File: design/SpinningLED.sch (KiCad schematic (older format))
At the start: 26 parts, among them IC1 4069, IC2 4017, P1 +, P2 -, SW1 SW_PUSH

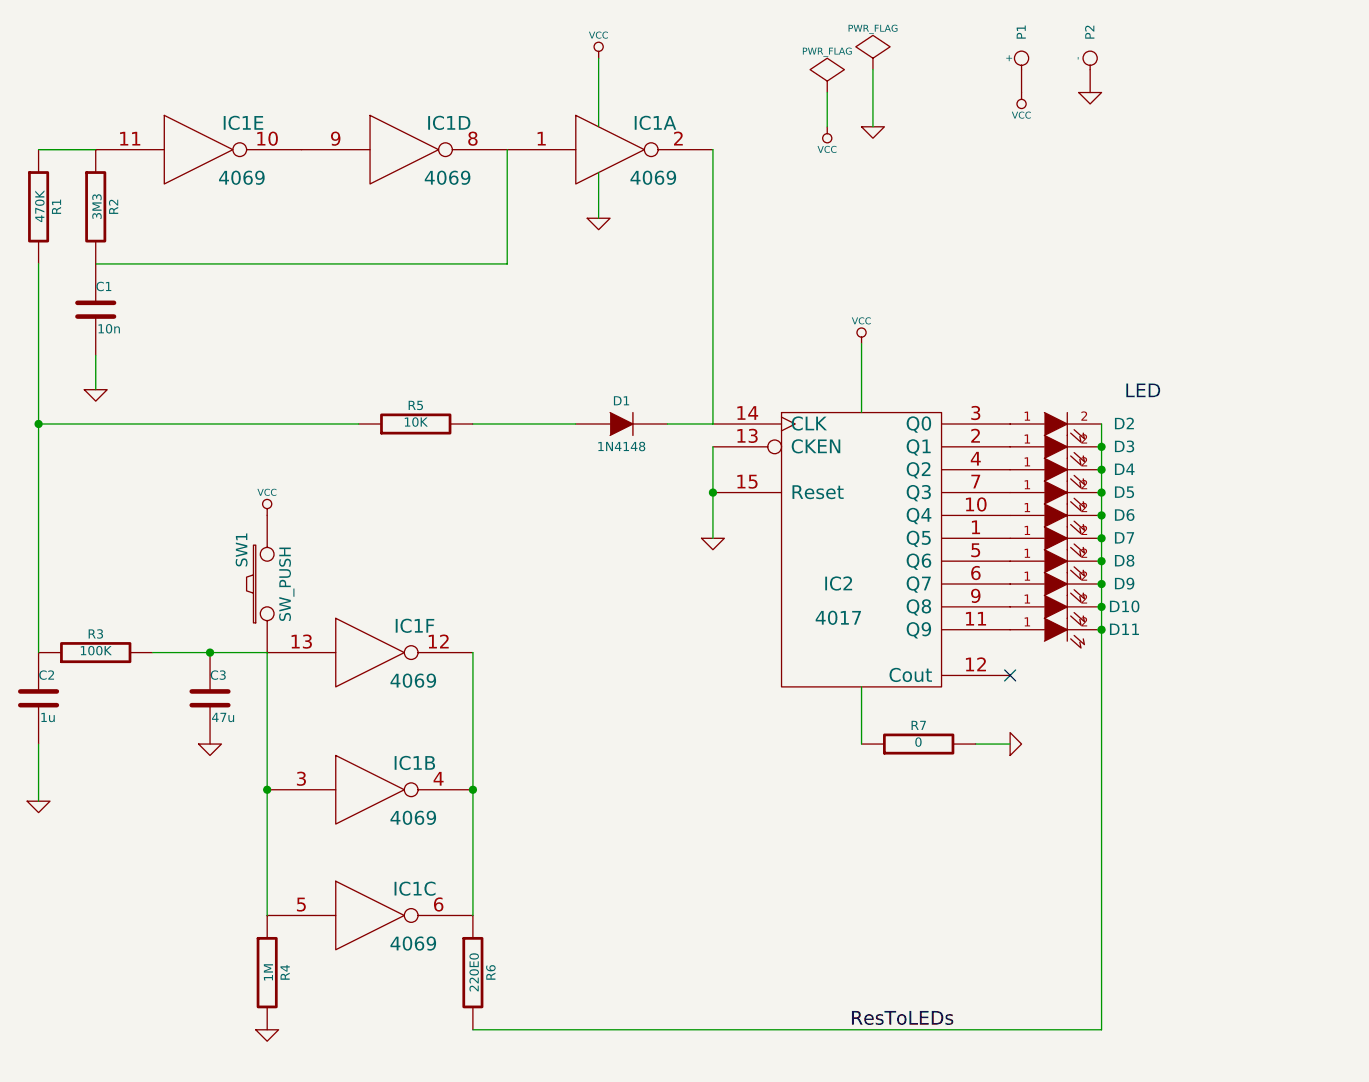
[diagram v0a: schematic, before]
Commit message: Routed traces complete
Also removed R7 - 0 ohm resistor
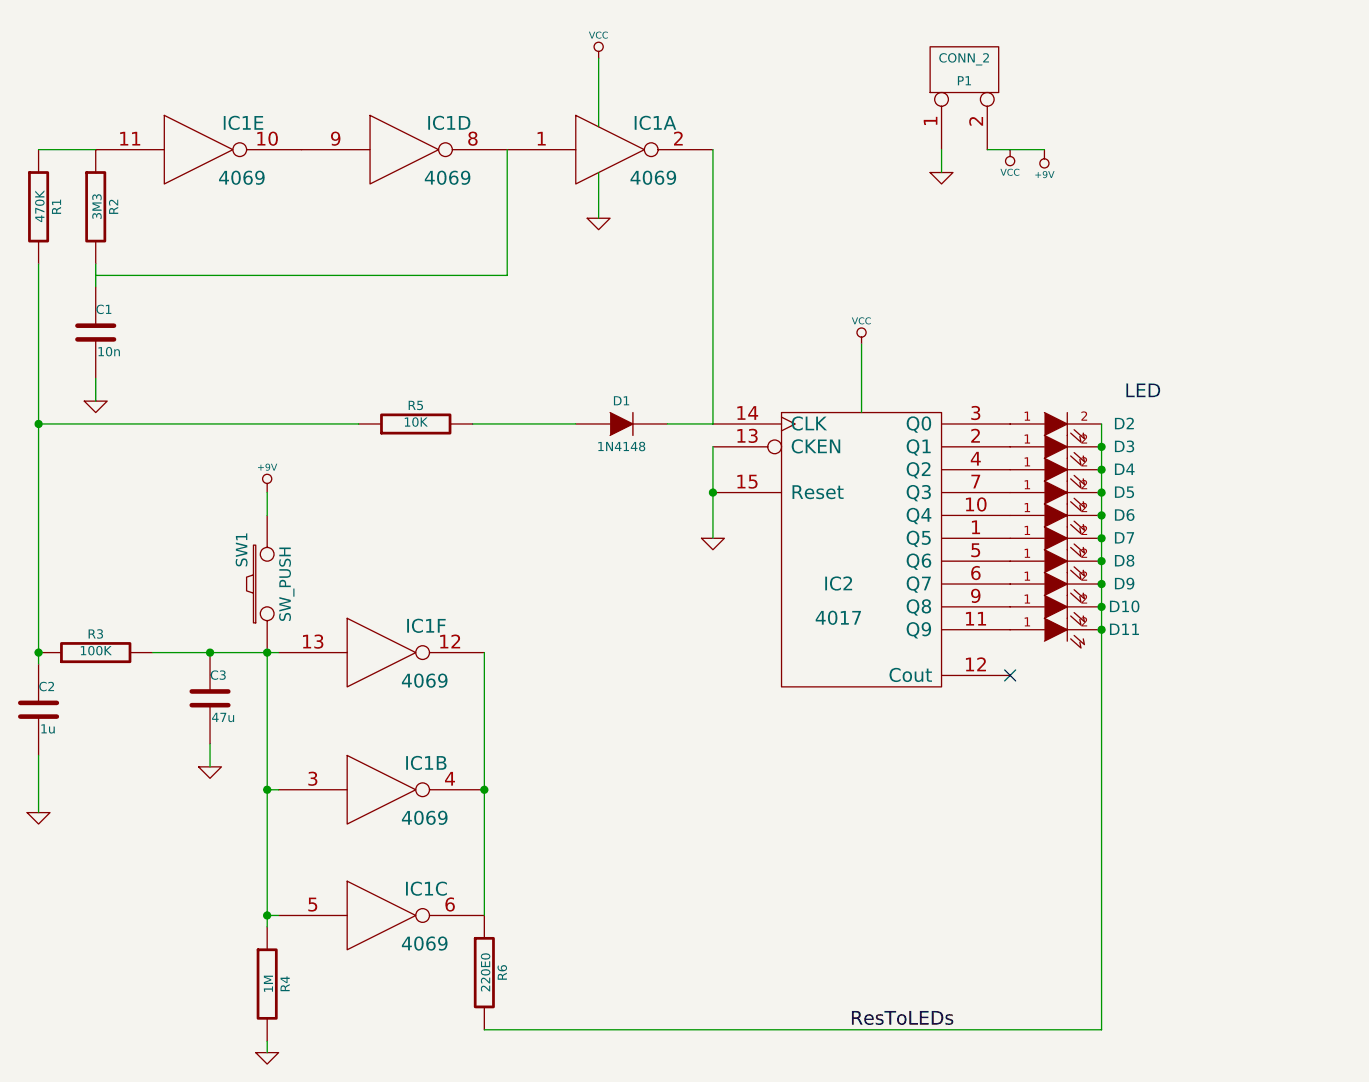
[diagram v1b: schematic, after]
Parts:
- removed P1: +, symbol CONN_1
- removed P2: -, symbol CONN_1
- removed R7: 0, R4, symbol R
- added P1: CONN_2, symbol CONN_2
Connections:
- net GND: now also P1.1 (P1)
- net VCC: no longer SW1.2
- net at IC1.1, IC1.8: no longer C1.1, R2.2
- new net: C1.1, R2.2
- new net +9V: P1.2 (PM), SW1.2
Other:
- moved on the sheet: C1, C2, IC1B, IC1C, IC1F, R4, R6

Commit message: SpinningLED v3
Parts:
- renumbered P1 to 9V+1
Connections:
- net ResToLEDs is gone; now on net GND: D10.2 (K), D11.2 (K), D2.2 (K), D3.2 (K), D4.2 (K), D5.2 (K), D6.2 (K), D7.2 (K), D8.2 (K), D9.2 (K), R6.2
- net +9V: now also C3.1, IC1.13, IC1.3, IC1.5, R3.2, R4.1; no longer 9V+1.2 (PM)
- net VCC: now also 9V+1.2 (PM), SW1.1
- net at IC1.1, IC1.8: now also C1.1, R2.2
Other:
- moved on the sheet: C2, SW1
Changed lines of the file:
@@
 LIBS:contrib
 LIBS:valves
+LIBS:battery-holder
 LIBS:SpinningLED-cache
 EELAYER 24 0
@@
 L C C2
 U 1 1 521A95A7
-P 1350 3850
-F 0 "C2" H 1350 3950 40  0000 L CNN
-F 1 "1u" H 1356 3765 40  0000 L CNN
-F 2 "C1" H 1388 3700 30  0001 C CNN
-F 3 "~" H 1350 3850 60  0000 C CNN
-	1    1350 3850
+P 1350 3950
+F 0 "C2" H 1350 4050 40  0000 L CNN
+F 1 "1u" H 1356 3865 40  0000 L CNN
+F 2 "C1" H 1388 3800 30  0001 C CNN
+F 3 "~" H 1350 3950 60  0000 C CNN
+	1    1350 3950
 	1    0    0    -1
 $EndComp
@@
 L GND #PWR02
 U 1 1 521A97B7
-P 1350 4300
-F 0 "#PWR02" H 1350 4300 30  0001 C CNN
-F 1 "GND" H 1350 4230 30  0001 C CNN
-F 2 "" H 1350 4300 60  0000 C CNN
-F 3 "" H 1350 4300 60  0000 C CNN
-	1    1350 4300
+P 1350 4400
+F 0 "#PWR02" H 1350 4400 30  0001 C CNN
+F 1 "GND" H 1350 4330 30  0001 C CNN
+F 2 "" H 1350 4400 60  0000 C CNN
+F 3 "" H 1350 4400 60  0000 C CNN
+	1    1350 4400
 	1    0    0    -1
 $EndComp
@@
 L SW_PUSH SW1
 U 1 1 521AA603
-P 2350 3300
-F 0 "SW1" H 2500 3410 50  0000 C CNN
-F 1 "SW_PUSH" H 2350 3220 50  0000 C CNN
-F 2 "SW_PUSH_SMALL" H 2350 3300 60  0001 C CNN
-F 3 "~" H 2350 3300 60  0000 C CNN
-	1    2350 3300
-	0    -1   -1   0
+P 6500 1250
+F 0 "SW1" H 6650 1360 50  0000 C CNN
+F 1 "SW_PUSH" H 6500 1170 50  0000 C CNN
+F 2 "SW_PUSH_SMALL" H 6500 1250 60  0001 C CNN
+F 3 "~" H 6500 1250 60  0000 C CNN
+	1    6500 1250
+	1    0    0    -1
 $EndComp
 $Comp
@@
 LED
 NoConn ~ 5600 3700
-Text Label 4900 5250 0    60   ~ 0
-ResToLEDs
-$Comp
-L VCC #PWR09
-U 1 1 52225733
-P 5600 1400
-F 0 "#PWR09" H 5600 1500 30  0001 C CNN
-F 1 "VCC" H 5600 1500 30  0000 C CNN
-F 2 "" H 5600 1400 60  0000 C CNN
-F 3 "" H 5600 1400 60  0000 C CNN
-	1    5600 1400
-	-1   0    0    1
-$EndComp
-$Comp
-L CONN_2 P1
+$Comp
+L CONN_2 9V+1
 U 1 1 522B9AE6
 P 5400 1050
-F 0 "P1" V 5350 1050 40  0000 C CNN
+F 0 "9V+1" V 5350 1050 40  0000 C CNN
 F 1 "CONN_2" V 5450 1050 40  0000 C CNN
 F 2 "" H 5400 1050 60  0000 C CNN
@@
 $EndComp
 $Comp
-L GND #PWR011
+L GND #PWR09
 U 1 1 522B9AFA
 P 5300 1500
-F 0 "#PWR011" H 5300 1500 30  0001 C CNN
+F 0 "#PWR09" H 5300 1500 30  0001 C CNN
 F 1 "GND" H 5300 1430 30  0001 C CNN
 F 2 "" H 5300 1500 60  0000 C CNN
@@
 	1    0    0    -1
 $EndComp
-$Comp
-L +9V #PWR012
-U 1 1 522B9B81
-P 5750 1400
-F 0 "#PWR012" H 5750 1370 20  0001 C CNN
-F 1 "+9V" H 5750 1510 30  0000 C CNN
-F 2 "" H 5750 1400 60  0000 C CNN
-F 3 "" H 5750 1400 60  0000 C CNN
-	1    5750 1400
-	-1   0    0    1
-$EndComp
-$Comp
-L +9V #PWR013
-U 1 1 522BA3A1
-P 2350 2900
-F 0 "#PWR013" H 2350 2870 20  0001 C CNN
-F 1 "+9V" H 2350 3010 30  0000 C CNN
-F 2 "" H 2350 2900 60  0000 C CNN
-F 3 "" H 2350 2900 60  0000 C CNN
-	1    2350 2900
-	1    0    0    -1
-$EndComp
 Wire Wire Line
 	2750 2600 1350 2600
 Connection ~ 1350 2600
 Wire Wire Line
-	1850 3600 2400 3600
-Wire Wire Line
-	2350 3600 2350 4800
+	1850 3600 2100 3600
+Wire Wire Line
+	2100 3600 2350 3600
+Wire Wire Line
+	2350 3600 2400 3600
+Wire Wire Line
+	2350 3250 2350 3600
+Wire Wire Line
+	2350 3600 2350 4200
+Wire Wire Line
+	2350 4200 2350 4750
+Wire Wire Line
+	2350 4750 2350 4800
 Connection ~ 2350 4200
 Wire Wire Line
-	3300 3600 3300 4750
+	3300 3600 3300 4200
+Wire Wire Line
+	3300 4200 3300 4750
 Connection ~ 3300 4200
 Wire Wire Line
-	1350 1900 1350 3650
+	1350 1900 1350 2600
+Wire Wire Line
+	1350 2600 1350 3600
+Wire Wire Line
+	1350 3600 1350 3750
 Wire Wire Line
 	3800 1500 3800 1700
@@
 	4300 2600 4300 1400
 Wire Wire Line
-	4300 2700 4300 3100
+	4300 2700 4300 2900
+Wire Wire Line
+	4300 2900 4300 3100
 Connection ~ 4300 2900
 Wire Wire Line
@@
 	4950 2550 4950 2250
 Wire Wire Line
-	6000 2600 6000 5250
+	6000 2600 6000 2700
+Wire Wire Line
+	6000 2700 6000 2800
+Wire Wire Line
+	6000 2800 6000 2900
+Wire Wire Line
+	6000 2900 6000 3000
+Wire Wire Line
+	6000 3000 6000 3100
+Wire Wire Line
+	6000 3100 6000 3200
+Wire Wire Line
+	6000 3200 6000 3300
+Wire Wire Line
+	6000 3300 6000 3400
+Wire Wire Line
+	6000 3400 6000 3500
+Wire Wire Line
+	6000 3500 6000 5250
 Connection ~ 6000 2700
 Connection ~ 6000 2800
@@
 Connection ~ 2100 3600
 Wire Wire Line
-	1350 4050 1350 4300
-Wire Wire Line
-	5500 1400 5750 1400
+	1350 4150 1350 4400
 Wire Wire Line
 	5300 1400 5300 1500
-Wire Wire Line
-	2350 2900 2350 3000
 Wire Wire Line
 	2100 4000 2100 4100
@@
 	3400 1950 3400 1400
 Wire Wire Line
-	1600 2000 1600 1900
+	1600 2000 1600 1950
+Wire Wire Line
+	1600 1950 1600 1900
+$Comp
+L VCC #PWR010
+U 1 1 527FFC21
+P 6100 1250
+F 0 "#PWR010" H 6100 1350 30  0001 C CNN
+F 1 "VCC" H 6100 1350 30  0000 C CNN
+F 2 "" H 6100 1250 60  0000 C CNN
+F 3 "" H 6100 1250 60  0000 C CNN
+	1    6100 1250
+	0    -1   -1   0
+$EndComp
+Wire Wire Line
+	5500 1400 5500 1500
+$Comp
+L GND #PWR011
+U 1 1 527FFF53
+P 4950 4050
+F 0 "#PWR011" H 4950 4050 30  0001 C CNN
+F 1 "GND" H 4950 3980 30  0001 C CNN
+F 2 "" H 4950 4050 60  0000 C CNN
+F 3 "" H 4950 4050 60  0000 C CNN
+	1    4950 4050
+	1    0    0    -1
+$EndComp
+Wire Wire Line
+	4950 3750 4950 4050
+$Comp
+L +9V #PWR012
+U 1 1 5280037F
+P 6950 1250
+F 0 "#PWR012" H 6950 1220 20  0001 C CNN
+F 1 "+9V" H 6950 1360 30  0000 C CNN
+F 2 "" H 6950 1250 60  0000 C CNN
+F 3 "" H 6950 1250 60  0000 C CNN
+	1    6950 1250
+	0    1    1    0
+$EndComp
+Wire Wire Line
+	6800 1250 6950 1250
+Wire Wire Line
+	6200 1250 6100 1250
+$Comp
+L +9V #PWR013
+U 1 1 52803867
+P 2350 3250
+F 0 "#PWR013" H 2350 3220 20  0001 C CNN
+F 1 "+9V" H 2350 3360 30  0000 C CNN
+F 2 "" H 2350 3250 60  0000 C CNN
+F 3 "" H 2350 3250 60  0000 C CNN
+	1    2350 3250
+	1    0    0    -1
+$EndComp
+$Comp
+L VCC #PWR014
+U 1 1 528038B4
+P 5500 1500
+F 0 "#PWR014" H 5500 1600 30  0001 C CNN
+F 1 "VCC" H 5500 1600 30  0000 C CNN
+F 2 "" H 5500 1500 60  0000 C CNN
+F 3 "" H 5500 1500 60  0000 C CNN
+	1    5500 1500
+	-1   0    0    1
+$EndComp
+Connection ~ 1600 1950
+Connection ~ 3400 1400
+Connection ~ 4300 2600
+Connection ~ 2500 1400
+Text Label 4900 5250 0    60   ~ 0
+GND
 $EndSCHEMATC
